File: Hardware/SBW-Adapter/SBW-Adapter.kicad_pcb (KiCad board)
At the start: 2 copper layers, 19 x 19 mm, 5 parts, among them J1 JTAG, J2 SpyBiWire, SW1 SW_SPDT

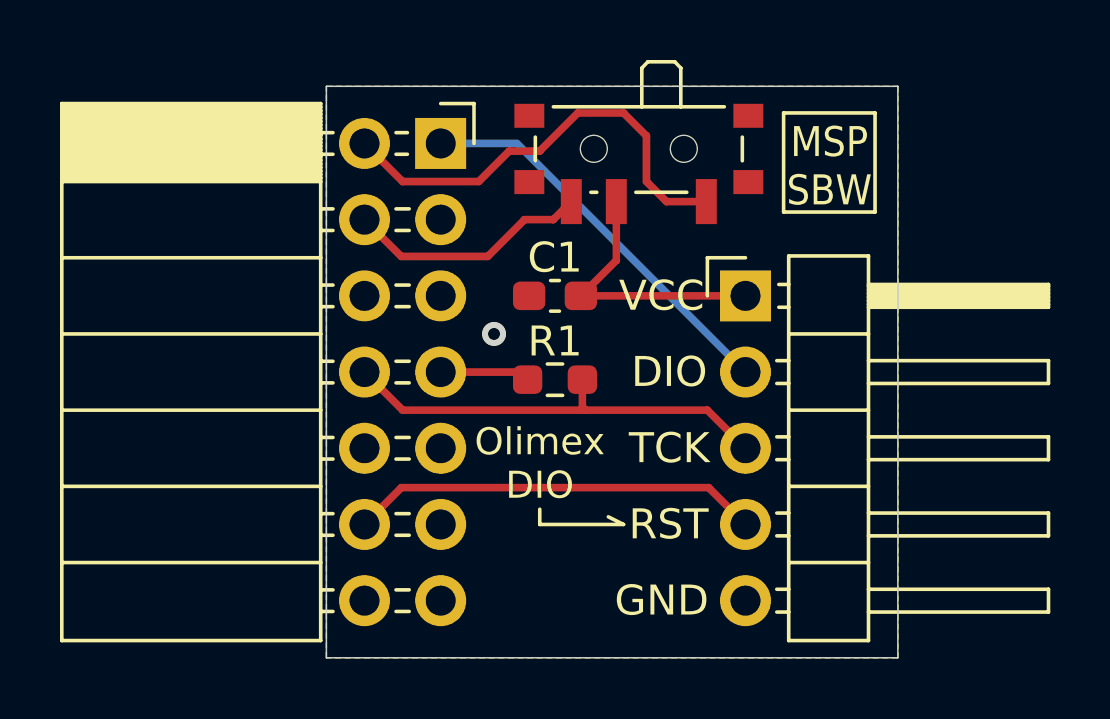
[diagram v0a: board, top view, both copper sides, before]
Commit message: Files for PCB Manufacturing of 4 boards. Preparation for Board documentation
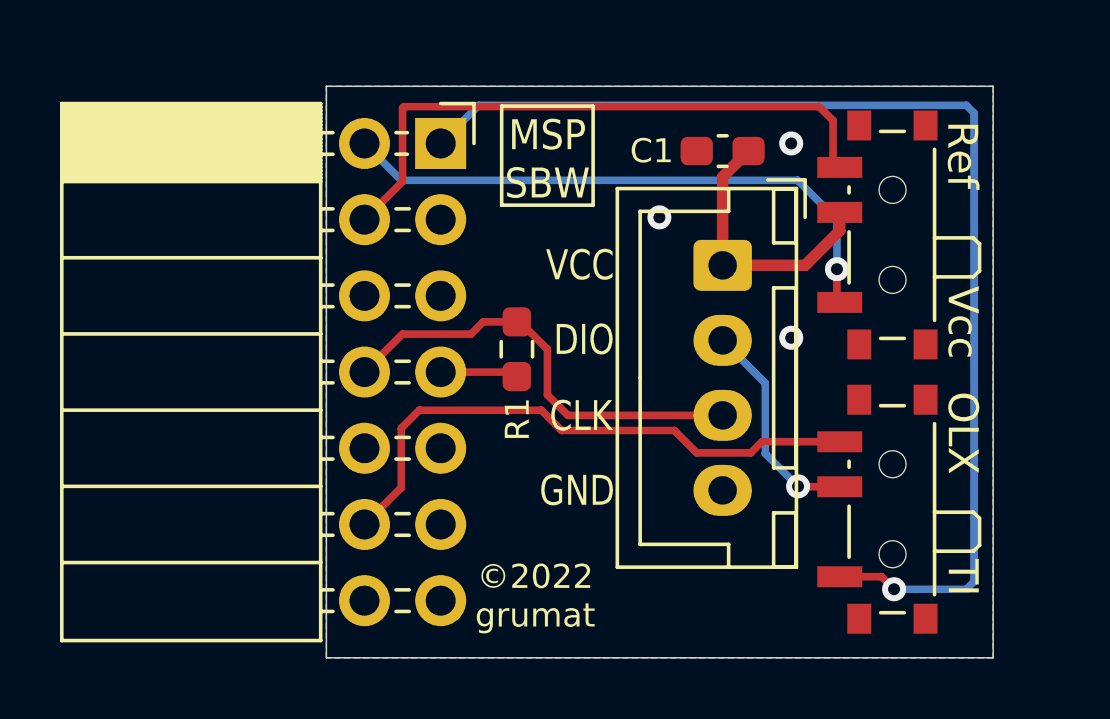
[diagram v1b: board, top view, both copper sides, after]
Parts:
- added SW2: TI_OLX, Button_Switch_SMD:SW_SPDT_PCM12, F.Cu at (126.5, 93.5)
- J2: footprint Connector_PinHeader_2.54mm:PinHeader_1x05_P2.54mm_Horizontal -> Connector_JST:JST_XH_B4B-XH-A_1x04_P2.50mm_Vertical
- SW1: value SW_SPDT -> PWR_SEL
- moved SW1 8.52 mm to (126.5, 84.3), turned to 90 degrees
- moved C1 7.38 mm to (121.2, 81.5)
- moved R1 1.63 mm to (114.3, 88.1), turned to -90 degrees
- moved J2 1.27 mm to (121.2, 85.3), turned to -90 degrees
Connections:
- net Net-(J1-Pad4) renamed /VREF
- J2 pad 2: /SBWTDOI -> /DOI
- J2 pad 4: /RST -> GND
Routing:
- net /SBWTDOI: track 13.3 -> 38.8 mm, vias 0 -> 1
- net /VREF: track 8.16 -> 20.5 mm
- net /DOI: track 0.00 -> 7.30 mm, vias 0 -> 1
- net /RST: track 13.7 -> 19.3 mm
- net +3.3V: track 15.0 -> 19.6 mm, vias 0 -> 1
- net GND: vias 1 -> 3
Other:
- board size 19 x 19 mm -> 22.2 x 19 mm
- board text added: "CLK"
- board text added: "OLX"
- board text added: "Ref"
- board text added: "TI"
- board text added: "Vcc"
- board text added: "©2022 grumat"
- board text removed: "Olimex DIO"
- board text removed: "RST"
- board text removed: "TCK"

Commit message: Fixed an error on the Olimex SBW layout
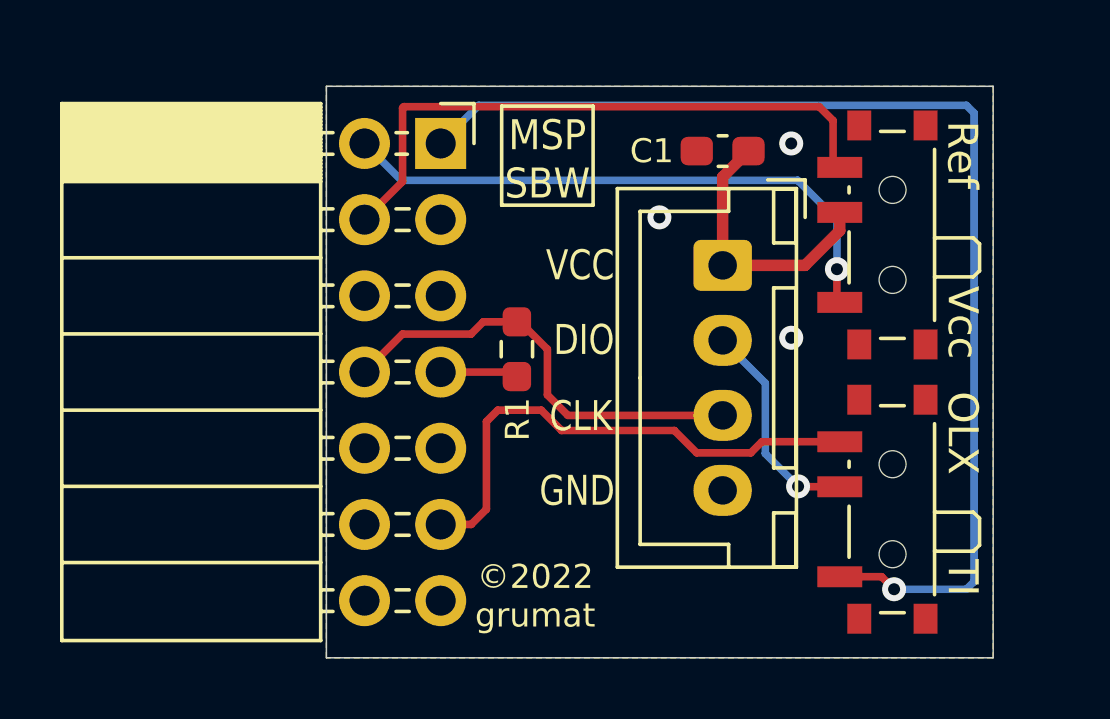
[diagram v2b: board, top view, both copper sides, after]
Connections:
- J1 pad 11: unconnected-(J1-Pad11) -> /RST
- J1 pad 12: /RST -> unconnected-(J1-Pad12)
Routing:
- net /RST: track 19.3 -> 17.3 mm
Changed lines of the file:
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@@
   (net 8 "GND")
   (net 9 "unconnected-(J1-Pad10)")
-  (net 10 "unconnected-(J1-Pad11)")
+  (net 10 "unconnected-(J1-Pad12)")
   (net 11 "/RST")
   (net 12 "unconnected-(J1-Pad13)")
@@
       (net 9 "unconnected-(J1-Pad10)") (pinfunction "Pin_10") (pintype "passive+no_connect"))
     (pad "11" thru_hole oval locked (at 0 12.7) (size 1.7 1.7) (drill 1) (layers *.Cu *.Mask)
-      (net 10 "unconnected-(J1-Pad11)") (pinfunction "Pin_11") (pintype "passive+no_connect"))
+      (net 11 "/RST") (pinfunction "Pin_11") (pintype "passive"))
     (pad "12" thru_hole oval locked (at -2.54 12.7) (size 1.7 1.7) (drill 1) (layers *.Cu *.Mask)
-      (net 11 "/RST") (pinfunction "Pin_12") (pintype "passive"))
+      (net 10 "unconnected-(J1-Pad12)") (pinfunction "Pin_12") (pintype "passive+no_connect"))
     (pad "13" thru_hole oval locked (at 0 15.24) (size 1.7 1.7) (drill 1) (layers *.Cu *.Mask)
       (net 12 "unconnected-(J1-Pad13)") (pinfunction "Pin_13") (pintype "passive+no_connect"))
@@
   (via (at 123.444 81.28) (size 0.8) (drill 0.4) (layers "F.Cu" "B.Cu") (free) (net 8))
   (segment (start 122.4682 91.222) (end 122.0978 91.5924) (width 0.254) (layer "F.Cu") (net 11))
-  (segment (start 110.447 92.753) (end 109.22 93.98) (width 0.254) (layer "F.Cu") (net 11))
+  (segment (start 113.284 90.551) (end 113.284 93.472) (width 0.254) (layer "F.Cu") (net 11))
+  (segment (start 113.664218 90.170782) (end 113.284 90.551) (width 0.254) (layer "F.Cu") (net 11))
+  (segment (start 120.2944 91.5924) (end 119.55 90.848) (width 0.254) (layer "F.Cu") (net 11))
+  (segment (start 115.112018 90.170782) (end 113.664218 90.170782) (width 0.254) (layer "F.Cu") (net 11))
+  (segment (start 115.789236 90.848) (end 115.112018 90.170782) (width 0.254) (layer "F.Cu") (net 11))
+  (segment (start 113.284 93.472) (end 112.776 93.98) (width 0.254) (layer "F.Cu") (net 11))
+  (segment (start 119.55 90.848) (end 115.789236 90.848) (width 0.254) (layer "F.Cu") (net 11))
   (segment (start 122.0978 91.5924) (end 120.2944 91.5924) (width 0.254) (layer "F.Cu") (net 11))
-  (segment (start 115.112018 90.170782) (end 111.048018 90.170782) (width 0.254) (layer "F.Cu") (net 11))
-  (segment (start 111.048018 90.170782) (end 110.447 90.7718) (width 0.254) (layer "F.Cu") (net 11))
-  (segment (start 115.789236 90.848) (end 115.112018 90.170782) (width 0.254) (layer "F.Cu") (net 11))
-  (segment (start 120.2944 91.5924) (end 119.55 90.848) (width 0.254) (layer "F.Cu") (net 11))
+  (segment (start 112.776 93.98) (end 111.76 93.98) (width 0.254) (layer "F.Cu") (net 11))
   (segment (start 125.062 91.222) (end 122.4682 91.222) (width 0.254) (layer "F.Cu") (net 11))
-  (segment (start 110.447 90.7718) (end 110.447 92.753) (width 0.254) (layer "F.Cu") (net 11))
-  (segment (start 119.55 90.848) (end 115.789236 90.848) (width 0.254) (layer "F.Cu") (net 11))
   (segment (start 125.062 84.188353) (end 123.906353 85.344) (width 0.381) (layer "F.Cu") (net 14))
   (segment (start 121.158 82.3965) (end 122.0205 81.534) (width 0.381) (layer "F.Cu") (net 14))

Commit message: Review of SBW-Adapter
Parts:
- SW1, SW2: footprint Button_Switch_SMD:SW_SPDT_PCM12 -> lib:SW_SPDT_PCM12
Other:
- board text added: "MSP SBW V2"
- board text removed: "MSP SBW"
